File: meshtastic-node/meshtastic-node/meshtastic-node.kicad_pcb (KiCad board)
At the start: 2 copper layers, 37 parts, among them J1 USB_C_Receptacle_USB2.0, J3 Conn_ARM_SWD_TagConnect_TC203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, J4 Conn_01x02_Pin, J5 Conn_Coaxial, U1 nRF52840, U2 TPS61222DCK, Y1 32MHz, Y2 32.768kHz

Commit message: changes
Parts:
- removed C15: 1uF, Capacitor_SMD:C_0805_2012Metric_Pad1.18x1.45mm_HandSolder
- removed C17: 12pF, Capacitor_SMD:C_0805_2012Metric_Pad1.18x1.45mm_HandSolder
- removed C21: 0.8pF, Capacitor_SMD:C_0805_2012Metric_Pad1.18x1.45mm_HandSolder
- removed C24: 100nF, Capacitor_SMD:C_0805_2012Metric_Pad1.18x1.45mm_HandSolder
- removed D4: PRTR5V0U2X, Package_TO_SOT_SMD:SOT-143
- removed L3: 10uH, Inductor_SMD:L_0805_2012Metric_Pad1.15x1.40mm_HandSolder
- removed L4: 4.1nH, Inductor_SMD:L_0805_2012Metric_Pad1.15x1.40mm_HandSolder
- removed Y1: 32MHz, Crystal:Crystal_SMD_SeikoEpson_FA238V-4Pin_3.2x2.5mm
- removed Y2: 32.768kHz, Crystal:Crystal_SMD_SeikoEpson_FA238V-4Pin_3.2x2.5mm
- added AE3: Antenna_Shield, RF_Antenna:Texas_SWRA117D_2.4GHz_Right, F.Cu at (129.2, 112.0)
- added C20: 220nF, Capacitor_SMD:C_0805_2012Metric_Pad1.18x1.45mm_HandSolder, F.Cu at (132.6, 94.0)
- added C25: 220pF, Capacitor_SMD:C_0805_2012Metric_Pad1.18x1.45mm_HandSolder, F.Cu at (137.4, 75.9)
- added C26: 470pF, Capacitor_SMD:C_0805_2012Metric_Pad1.18x1.45mm_HandSolder, F.Cu at (137.4, 78.9)
- added C27: 4700pF, Capacitor_SMD:C_0805_2012Metric_Pad1.18x1.45mm_HandSolder, F.Cu at (137.4, 81.9)
- added C28: 0.047uF, Capacitor_SMD:C_0805_2012Metric_Pad1.18x1.45mm_HandSolder, F.Cu at (137.4, 84.9)
- added C29: 470pF, Capacitor_SMD:C_0805_2012Metric_Pad1.18x1.45mm_HandSolder, F.Cu at (137.4, 87.9)
- added C30: 220pF, Capacitor_SMD:C_0805_2012Metric_Pad1.18x1.45mm_HandSolder, F.Cu at (137.4, 90.9)
- added C31: 1.0pF, Capacitor_SMD:C_0805_2012Metric_Pad1.18x1.45mm_HandSolder, F.Cu at (137.4, 94.0)
- added C34: 10uF, Capacitor_SMD:C_0805_2012Metric_Pad1.18x1.45mm_HandSolder, F.Cu at (142.3, 69.9)
- added C35: 10uF, Capacitor_SMD:C_0805_2012Metric_Pad1.18x1.45mm_HandSolder, F.Cu at (142.3, 72.9)
- added C36: 100pF, Capacitor_SMD:C_0805_2012Metric_Pad1.18x1.45mm_HandSolder, F.Cu at (142.3, 75.9)
- added C37: 1uF, Capacitor_SMD:C_0805_2012Metric_Pad1.18x1.45mm_HandSolder, F.Cu at (142.3, 78.9)
- added C38: 22uF, Capacitor_SMD:C_0805_2012Metric_Pad1.18x1.45mm_HandSolder, F.Cu at (142.3, 81.9)
- added C39: 22uF, Capacitor_SMD:C_0805_2012Metric_Pad1.18x1.45mm_HandSolder, F.Cu at (142.3, 84.9)
- added C40: 1uF, Capacitor_SMD:C_0805_2012Metric_Pad1.18x1.45mm_HandSolder, F.Cu at (142.3, 87.9)
- added D1: LED, LED_SMD:LED_0805_2012Metric_Pad1.15x1.40mm_HandSolder, F.Cu at (165.1, 103.9)
- added D2: LED, LED_SMD:LED_0805_2012Metric_Pad1.15x1.40mm_HandSolder, F.Cu at (165.1, 106.9)
- added D3: LED, LED_SMD:LED_0805_2012Metric_Pad1.15x1.40mm_HandSolder, F.Cu at (165.1, 109.9)
- added D5: LED, LED_SMD:LED_0805_2012Metric_Pad1.15x1.40mm_HandSolder, F.Cu at (165.1, 113.0)
- added IC4: TPS2121RUXT, TPS:TPS2121RUXT, F.Cu at (147.1, 118.3)
- added IC7: TPS2121RUXT, TPS:TPS2121RUXT, F.Cu at (152.0, 118.3)
- added J2: Conn_01x05_Socket, Connector_JST:JST_EH_S5B-EH_1x05_P2.50mm_Horizontal, F.Cu at (105.3, 102.0)
- added J6: Conn_ARM_JTAG_SWD_10, Connector_PinHeader_1.27mm:PinHeader_2x05_P1.27mm_Vertical, F.Cu at (169.6, 113.6)
- added L6: 3.9nH, Inductor_SMD:L_0805_2012Metric_Pad1.15x1.40mm_HandSolder, F.Cu at (147.0, 75.7)
- added L7: 4.7nH, Inductor_SMD:L_0805_2012Metric_Pad1.15x1.40mm_HandSolder, F.Cu at (147.0, 78.7)
- added L9: 4.7uH, Inductor_SMD:L_0805_2012Metric_Pad1.15x1.40mm_HandSolder, F.Cu at (147.0, 81.6)
- added Q1: PMOS, Package_TO_SOT_SMD:SOT-23_Handsoldering, F.Cu at (170.7, 104.8)
- added Q2: PMOS, Package_TO_SOT_SMD:SOT-23_Handsoldering, F.Cu at (170.7, 109.6)
- added R1: 6.8k, Resistor_SMD:R_0805_2012Metric_Pad1.20x1.40mm_HandSolder, F.Cu at (147.0, 84.6)
- added R10: 120, Resistor_SMD:R_0805_2012Metric_Pad1.20x1.40mm_HandSolder, F.Cu at (151.8, 87.5)
- added R11: 10k, Resistor_SMD:R_0805_2012Metric_Pad1.20x1.40mm_HandSolder, F.Cu at (151.8, 90.5)
- added R12: 51k, Resistor_SMD:R_0805_2012Metric_Pad1.20x1.40mm_HandSolder, F.Cu at (156.5, 69.8)
- added R13: 51.1k, Resistor_SMD:R_0805_2012Metric_Pad1.20x1.40mm_HandSolder, F.Cu at (156.5, 72.8)
- added R14: 1k, Resistor_SMD:R_0805_2012Metric_Pad1.20x1.40mm_HandSolder, F.Cu at (156.5, 75.7)
- added R16: 4.7k, Resistor_SMD:R_0805_2012Metric_Pad1.20x1.40mm_HandSolder, F.Cu at (156.5, 78.7)
- added R17: 4.7k, Resistor_SMD:R_0805_2012Metric_Pad1.20x1.40mm_HandSolder, F.Cu at (156.5, 81.6)
- added R18: 22k, Resistor_SMD:R_0805_2012Metric_Pad1.20x1.40mm_HandSolder, F.Cu at (156.5, 84.6)
- added R19: 4.7k, Resistor_SMD:R_0805_2012Metric_Pad1.20x1.40mm_HandSolder, F.Cu at (156.5, 87.5)
- added R2: 1k, Resistor_SMD:R_0805_2012Metric_Pad1.20x1.40mm_HandSolder, F.Cu at (147.0, 87.5)
- added R20: 100k, Resistor_SMD:R_0805_2012Metric_Pad1.20x1.40mm_HandSolder, F.Cu at (156.5, 90.5)
- added R21: 700k, Resistor_SMD:R_0805_2012Metric_Pad1.20x1.40mm_HandSolder, F.Cu at (161.3, 69.8)
- added R22: 4.7k, Resistor_SMD:R_0805_2012Metric_Pad1.20x1.40mm_HandSolder, F.Cu at (161.3, 72.8)
- added R23: 51.1k, Resistor_SMD:R_0805_2012Metric_Pad1.20x1.40mm_HandSolder, F.Cu at (161.3, 75.7)
- added R24: 4.7k, Resistor_SMD:R_0805_2012Metric_Pad1.20x1.40mm_HandSolder, F.Cu at (161.3, 78.7)
- added R25: 5k, Resistor_SMD:R_0805_2012Metric_Pad1.20x1.40mm_HandSolder, F.Cu at (161.3, 81.6)
- added R26: 23.7k, Resistor_SMD:R_0805_2012Metric_Pad1.20x1.40mm_HandSolder, F.Cu at (161.3, 84.6)
- added R27: 23.7k, Resistor_SMD:R_0805_2012Metric_Pad1.20x1.40mm_HandSolder, F.Cu at (161.3, 87.5)
- added R28: 23.7k, Resistor_SMD:R_0805_2012Metric_Pad1.20x1.40mm_HandSolder, F.Cu at (161.3, 90.5)
- added R29: 5k, Resistor_SMD:R_0805_2012Metric_Pad1.20x1.40mm_HandSolder, F.Cu at (166.0, 69.8)
- added R3: 1k, Resistor_SMD:R_0805_2012Metric_Pad1.20x1.40mm_HandSolder, F.Cu at (147.0, 90.5)
- added R30: 23.7k, Resistor_SMD:R_0805_2012Metric_Pad1.20x1.40mm_HandSolder, F.Cu at (166.0, 72.8)
- added R31: 5k, Resistor_SMD:R_0805_2012Metric_Pad1.20x1.40mm_HandSolder, F.Cu at (166.0, 75.7)
- added R32: 5k, Resistor_SMD:R_0805_2012Metric_Pad1.20x1.40mm_HandSolder, F.Cu at (166.0, 78.7)
- added R36: 0.1, Resistor_SMD:R_0805_2012Metric_Pad1.20x1.40mm_HandSolder, F.Cu at (166.0, 81.6)
- added R37: 0.1, Resistor_SMD:R_0805_2012Metric_Pad1.20x1.40mm_HandSolder, F.Cu at (166.0, 84.6)
- added R38: 0.1, Resistor_SMD:R_0805_2012Metric_Pad1.20x1.40mm_HandSolder, F.Cu at (166.0, 87.5)
- added R4: 10k, Resistor_SMD:R_0805_2012Metric_Pad1.20x1.40mm_HandSolder, F.Cu at (151.8, 69.8)
- added R5: 10k, Resistor_SMD:R_0805_2012Metric_Pad1.20x1.40mm_HandSolder, F.Cu at (151.8, 72.8)
- added R6: 10k, Resistor_SMD:R_0805_2012Metric_Pad1.20x1.40mm_HandSolder, F.Cu at (151.8, 75.7)
- added R7: 33.2k, Resistor_SMD:R_0805_2012Metric_Pad1.20x1.40mm_HandSolder, F.Cu at (151.8, 78.7)
- added R8: 0.1, Resistor_SMD:R_0805_2012Metric_Pad1.20x1.40mm_HandSolder, F.Cu at (151.8, 81.6)
- added R9: 10k, Resistor_SMD:R_0805_2012Metric_Pad1.20x1.40mm_HandSolder, F.Cu at (151.8, 84.6)
- added TP1: TestPoint, TestPoint:TestPoint_Pad_D2.0mm, F.Cu at (127.5, 115.0)
- added TP2: TestPoint, TestPoint:TestPoint_Pad_D2.0mm, F.Cu at (127.5, 119.0)
- added TP3: TestPoint, TestPoint:TestPoint_Pad_D2.0mm, F.Cu at (131.5, 115.0)
- added TP4: TestPoint, TestPoint:TestPoint_Pad_D2.0mm, F.Cu at (131.5, 119.0)
- added TP5: TestPoint, TestPoint:TestPoint_Pad_D2.0mm, F.Cu at (135.6, 115.0)
- added TP6: TestPoint, TestPoint:TestPoint_Pad_D2.0mm, F.Cu at (135.6, 119.0)
- added U3: TPS61222DCK, Package_TO_SOT_SMD:Texas_R-PDSO-G6, F.Cu at (139.7, 118.9)
- added U4: BME280, Package_LGA:Bosch_LGA-8_2.5x2.5mm_P0.65mm_ClockwisePinNumbering, F.Cu at (170.7, 87.1)
- added U5: INA3221, Package_DFN_QFN:Texas_RGV0016A_VQFN-16-1EP_4x4mm_P0.65mm_EP2.1x2.1mm, F.Cu at (171.6, 71.5)
- C1, C3: value 1uF -> 10uF
- C10, C11, C6: value 100nF -> 10uF
- C12: value 100nF -> 0.1uF
- C13: value 1uF -> 22uF
- C14: value 0.5pF -> 22uF
- C16: value 12pF -> 22uF
- C2: value 4.7uF -> 10uF
- C22, C23: value 12pF -> 100nF
- C4: value 47nF -> 100nF
- C5: value 4.7uF -> 100nF
- C7: value 100pF -> 10uF
- C8: value 820pF -> 10uF
- C9: value 4.7uF -> 1uF
- J3: value Conn_ARM_SWD_TagConnect_TC2030-NL -> Conn_Coaxial_Small; footprint Connector:Tag-Connect_TC2030-IDC-NL_2x03_P1.27mm_Vertical -> Connector_Coaxial:SMA_Molex_73251-1153_EdgeMount_Horizontal
- J4: value Conn_01x02_Pin -> Conn_01x02_Socket; footprint Connector_JST:JST_EH_B2B-EH-A_1x02_P2.50mm_Vertical -> Connector_JST:JST_EH_S2B-EH_1x02_P2.50mm_Horizontal
- J5: value Conn_Coaxial -> Conn_01x02_Socket; footprint Connector_Coaxial:U.FL_Hirose_U.FL-R-SMT-1_Vertical -> Connector_JST:JST_EH_S2B-EH_1x02_P2.50mm_Horizontal
- L1: value 10uH -> 2.2uH; footprint Inductor_SMD:L_0805_2012Metric_Pad1.15x1.40mm_HandSolder -> Inductor_SMD_Wurth:L_Wurth_WE-LQSH-4020
- L2: value 15nH -> 10uH
- U1: value nRF52840 -> TPS565208; footprint Package_DFN_QFN:Nordic_AQFN-73-1EP_7x7mm_P0.5mm -> Package_TO_SOT_SMD:SOT-23-6
- moved J3 97.1 mm to (198.4, 78.1)
- moved L1 73.6 mm to (171.3, 77.5)
- moved J1 70.2 mm to (169.6, 97.3)
- moved U1 68.6 mm to (171.0, 82.6)
- moved J4 63.3 mm to (148.2, 99.7)
- moved U2 57.0 mm to (139.7, 114.9)
- moved C9 50.8 mm to (127.8, 94.0)
- moved J5 49.8 mm to (157.7, 99.7)
- moved L2 47.7 mm to (147.0, 69.8)
- moved L5 47.2 mm to (147.0, 72.8)
- moved C18 45.2 mm to (132.6, 87.9)
- moved C19 45.2 mm to (132.6, 90.9)
- moved C1 43.5 mm to (127.8, 69.9)
- moved C2 43.5 mm to (127.8, 72.9)
- moved C3 43.5 mm to (127.8, 75.9)
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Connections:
- net +3V3 renamed Net-(IC3-ANT)
- net VBUS_IN renamed VBUS
- C1 pad 1: VBUS_MAIN -> VDD_NRF
- C10 pad 1: VDD_NRF -> Sys Load
- C11 pad 1: VDD_NRF -> Sys Load
- C12 pad 1: VDD_NRF -> Sys Load
- C13 pad 1: VDD_NRF -> GND
- C13 pad 2: GND -> VDD_NRF
- C14 pad 1: Net-(J5-In) -> GND
- C14 pad 2: GND -> VDD_NRF
- C16 pad 1: GND -> Net-(U1-VBST)
- C16 pad 2: Net-(U1-XC1) -> Net-(U1-SW)
- C18 pad 1: VSYS -> VDD_NRF
- C22 pad 2: Net-(U1-XL2/P0.01) -> VDD_NRF
- C23 pad 2: Net-(U1-XL1/P0.00) -> VDD_NRF
- C3 pad 1: Net-(U1-DEC4) -> VDD_NRF
- C4 pad 1: Net-(U1-DEC4) -> VDD_NRF
- C5 pad 1: Net-(U1-DECUSB) -> VDD_NRF
- C6 pad 1: Net-(U1-DEC1) -> VDD_NRF
- C7 pad 1: Net-(U1-DEC3) -> VDD_NRF
- C8 pad 1: Net-(U1-DEC5) -> VDD_NRF
- C9 pad 1: VDD_NRF -> Net-(IC1-VDD)
- J3 pad 2: SWDI -> GND
- J4 pad 1: Net-(J4-Pin_1) -> Bat Shunt 1
- J5 pad 1: Net-(J5-In) -> Sol Shunt 1
- L1 pad 1: Net-(L1-Pad1) -> Net-(U1-SW)
- L1 pad 2: Net-(U1-DCC) -> VDD_NRF
- L2 pad 1: Net-(U1-DEC4) -> Net-(D6-K)
- L2 pad 2: Net-(L1-Pad1) -> Net-(IC2-CSP)
- L5 pad 1: VSYS -> VDD_NRF
- U2 pad 1: VSYS -> VDD_NRF
- U2 pad 6: VSYS -> VDD_NRF

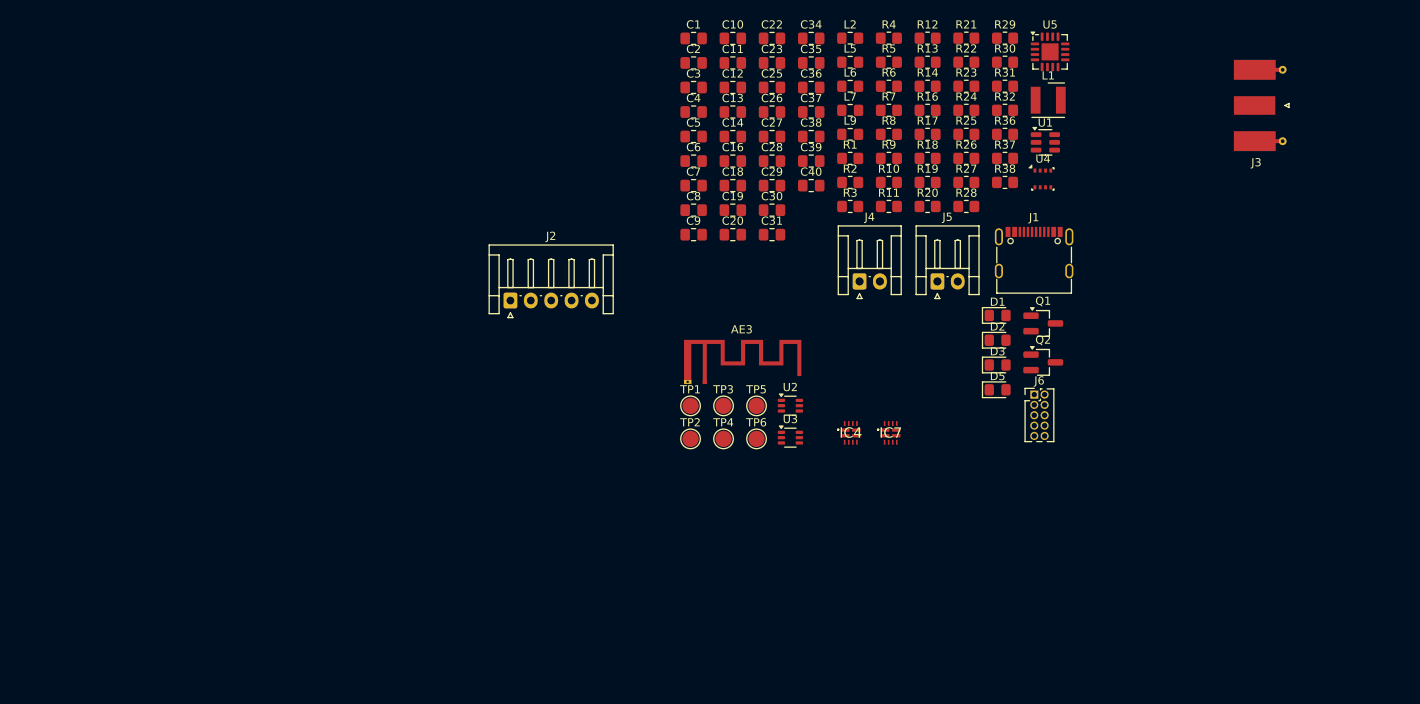
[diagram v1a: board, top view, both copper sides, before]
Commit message: Most component selection
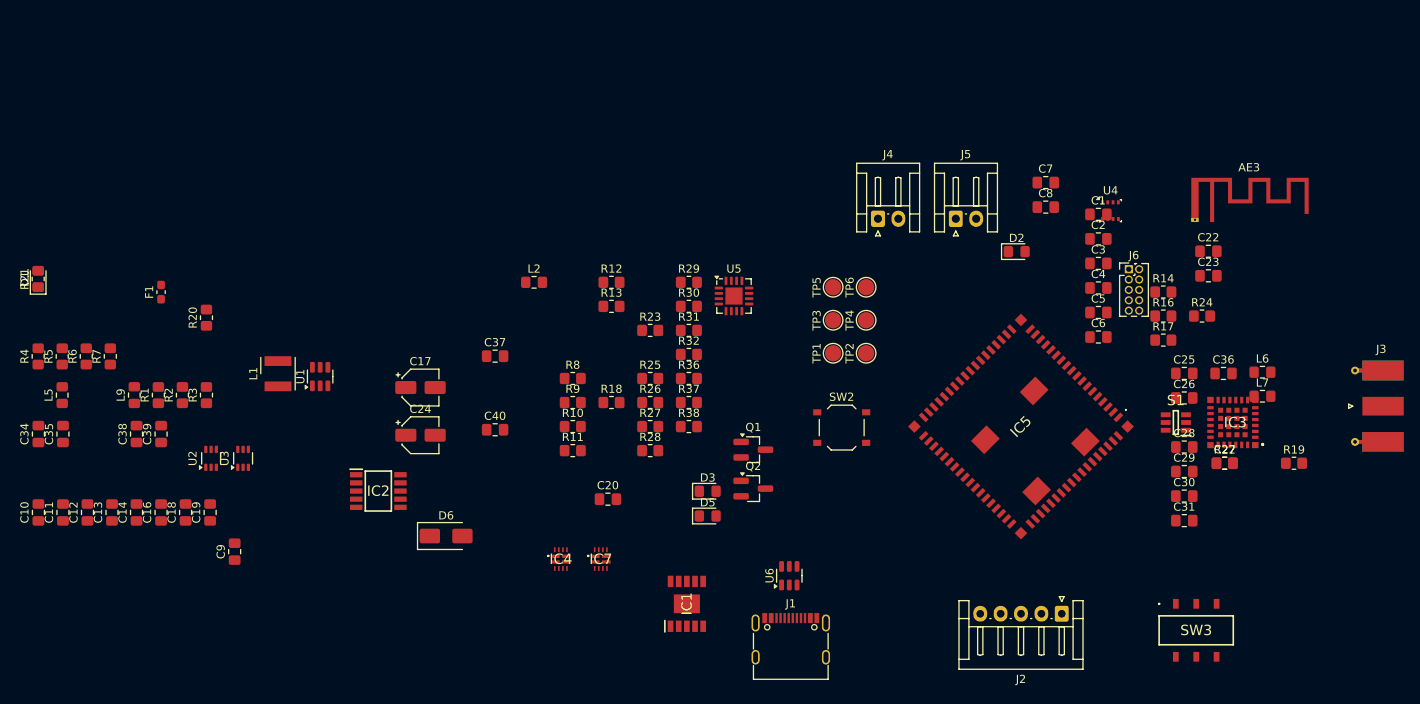
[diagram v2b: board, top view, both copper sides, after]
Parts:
- added C17: 10uF, Capacitor_SMD:CP_Elec_4x5.4, F.Cu at (94.3, 112.7)
- added C24: 100nF, Capacitor_SMD:CP_Elec_4x5.4, F.Cu at (94.3, 118.6)
- added D6: D_Schottky, Diode_SMD:D_SMA, F.Cu at (97.5, 130.9)
- added F1: Fuse (3A), Fuse:Fuse_0603_1608Metric_Pad1.05x0.95mm_HandSolder, F.Cu at (62.5, 101.0)
- added IC1: CH224K, meshtastic:SOP100P600X180-11N, F.Cu at (127.0, 139.2)
- added IC2: CN3791, meshtastic:SOP100P600X175-10N, F.Cu at (89.1, 125.4)
- added IC3: SKY65313-21, meshtastic:SKY6531321, F.Cu at (194.0, 117.0)
- added IC5: Wio-WM1110, meshtastic:WioWM1110, F.Cu at (168.0, 117.5)
- added S1: HMC544AETR, meshtastic:SOT95P280X145-6N, F.Cu at (187.0, 117.0)
- added SW2: SW_Push, Button_Switch_SMD:SW_Push_1P1T_XKB_TS-1187A, F.Cu at (146.0, 117.6)
- added SW3: SW_DPDT_x2, meshtastic:SS3235SL3, F.Cu at (189.5, 142.5)
- added U6: USBLC6-2SC6, Package_TO_SOT_SMD:SOT-23-6, F.Cu at (139.6, 135.8)
- moved D1 117.8 mm to (47.4, 99.4), turned to 90 degrees
- moved R21 117.7 mm to (47.4, 99.4), turned to 90 degrees
- moved R4 111.5 mm to (47.4, 108.9), turned to 90 degrees
- moved R5 107.7 mm to (50.4, 108.9), turned to 90 degrees
- moved C34 106.5 mm to (47.4, 118.4), turned to 90 degrees
- moved L5 105.0 mm to (50.4, 113.6), turned to 90 degrees
- moved R6 103.9 mm to (53.3, 108.9), turned to 90 degrees
- moved C10 103.2 mm to (47.4, 128.0), turned to 90 degrees
- moved C35 102.5 mm to (50.4, 118.4), turned to 90 degrees
- moved L1 100.3 mm to (76.8, 111.0), turned to 90 degrees
- moved R7 100.2 mm to (56.2, 108.9), turned to 90 degrees
- moved C11 99.0 mm to (50.4, 128.0), turned to 90 degrees
- moved C12 94.8 mm to (53.5, 128.0), turned to 90 degrees
- moved U1 93.5 mm to (82.0, 111.4), turned to 90 degrees
- moved L9 93.5 mm to (59.2, 113.6), turned to 90 degrees
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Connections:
- net D+ renamed Net-(J1-D+-PadA6)
- net D- renamed Net-(J1-D--PadA7)
- C10 pad 1: Sys Load -> Net-(U1-VIN)
- C11 pad 1: Sys Load -> Net-(U1-VIN)
- C12 pad 1: Sys Load -> Net-(U1-VIN)
- R5 pad 2: Sys Load -> Net-(U1-VIN)
- U1 pad 3: Sys Load -> Net-(U1-VIN)

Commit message: better part selection
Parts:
- L1: footprint Inductor_SMD_Wurth:L_Wurth_WE-LQSH-4020 -> Inductor_SMD:L_SXN_SMDRI124
- moved L1 9.58 mm to (78.0, 101.5)

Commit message: small rev
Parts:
- moved J1 181.2 mm to (-26.6, 72.9)
- moved U6 181.2 mm to (-26.8, 63.9)
- moved IC1 175.8 mm to (-27.5, 55.4)
- moved C9 133.6 mm to (-35.7, 53.2)
- moved R3 123.9 mm to (-40.2, 53.2)
- moved R1 122.0 mm to (-39.5, 46.3)
- moved R2 122.0 mm to (-36.6, 46.3)
- moved J5 108.6 mm to (52.4, 107.1), turned to 90 degrees
- moved J4 101.1 mm to (52.4, 116.7), turned to 90 degrees
- moved C13 98.0 mm to (47.2, 30.5), turned to 0 degrees
- moved U2 95.8 mm to (-27.1, 125.9)
- moved U3 95.8 mm to (-23.1, 125.9)
- moved C14 95.3 mm to (47.2, 33.5), turned to 0 degrees
- moved R20 90.5 mm to (-21.1, 119.5)
- moved C38 85.6 mm to (-26.0, 112.8)
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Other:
- board outline added: 150.1 x 50 mm

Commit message: test
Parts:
- moved R21 151.7 mm to (118.3, 96.7)
- moved L5 151.0 mm to (118.3, 104.1)
- moved U2 151.0 mm to (122.4, 104.2)
- moved L9 150.1 mm to (123.2, 94.4)
- moved C34 148.1 mm to (112.0, 97.9)
- moved C35 148.1 mm to (115.0, 97.9)
- moved C39 148.1 mm to (124.4, 98.7)
- moved C38 147.4 mm to (120.7, 98.8)
- moved R1 139.3 mm to (82.6, 113.4), turned to -90 degrees
- moved R20 138.9 mm to (115.9, 96.9)
- moved U3 138.9 mm to (113.9, 103.2)
- moved C18 138.2 mm to (119.0, 100.0)
- moved C19 138.2 mm to (122.0, 100.0)
- moved R3 138.0 mm to (86.3, 108.3), turned to 0 degrees
- moved R2 136.2 mm to (86.3, 104.9), turned to 180 degrees
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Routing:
- net VBUS: track 0.00 -> 29.2 mm
- net CC1: track 0.00 -> 13.2 mm
- net D+: track 0.00 -> 8.59 mm
- net D-: track 0.00 -> 8.32 mm
- net CC2: track 0.00 -> 7.82 mm
- net Net-(J1-D--PadA7): track 0.00 -> 6.80 mm
- net Net-(J1-D+-PadA6): track 0.00 -> 5.63 mm
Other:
- copper layers 2 -> 4

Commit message: routing
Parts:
- added J7: Conn_Coaxial_Small, Connector_Coaxial:SMA_Molex_73251-1153_EdgeMount_Horizontal, F.Cu at (178.6, 108.2)
- added REF**: MountingHole_2.2mm_M2_Pad_Via, MountingHole:MountingHole_2.2mm_M2_Pad_Via, F.Cu at (180.7, 118.6)
- added REF**: MountingHole_2.2mm_M2_Pad_Via, MountingHole:MountingHole_2.2mm_M2_Pad_Via, F.Cu at (35.8, 118.6)
- added REF**: MountingHole_2.2mm_M2_Pad_Via, MountingHole:MountingHole_2.2mm_M2_Pad_Via, F.Cu at (35.8, 73.7)
- added REF**: MountingHole_2.2mm_M2_Pad_Via, MountingHole:MountingHole_2.2mm_M2_Pad_Via, F.Cu at (180.7, 73.6)
- moved C1 98.8 mm to (83.7, 166.2)
- moved C2 98.8 mm to (83.7, 169.2)
- moved C5 98.8 mm to (74.7, 173.2)
- moved C6 98.8 mm to (74.7, 176.2)
- moved C7 98.8 mm to (79.2, 166.9)
- moved C8 98.8 mm to (79.4, 170.6)
- moved C3 98.8 mm to (74.7, 167.1)
- moved C4 98.8 mm to (74.7, 170.2)
- moved C22 86.2 mm to (114.3, 135.3)
- moved C23 86.2 mm to (114.3, 138.3)
- moved U4 85.4 mm to (112.6, 144.8)
- moved R16 75.8 mm to (109.7, 103.1)
- moved R17 75.8 mm to (109.7, 106.0)
- moved R24 75.8 mm to (114.4, 103.1)
- moved R12 64.9 mm to (48.6, 92.2), turned to 180 degrees
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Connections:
- C25 pad 1: +4V -> USE_ANT_2
- C26 pad 1: +4V -> USE_ANT_2
- C27 pad 1: +4V -> USE_ANT_2
- C28 pad 1: +4V -> USE_ANT_2
- IC3 pad 23: +4V -> USE_ANT_2
- IC3 pad 24: +4V -> USE_ANT_2
- IC3 pad 25: +4V -> USE_ANT_2
- IC3 pad 26: +4V -> USE_ANT_2
- SW3 pad 2: VDD_NRF -> +4V
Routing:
- net VDD_NRF: track 0.00 -> 13.3 mm
- added copper zone on B.Cu, net GND
- added copper zone on F.Cu, net GND
- added copper zone on In1.Cu, net GND
- added copper zone on In2.Cu, net GND
- added copper zone on In1.Cu, net VDD_NRF
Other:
- board size 150.1 x 50 mm -> 150 x 50 mm
